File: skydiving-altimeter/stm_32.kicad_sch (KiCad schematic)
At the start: 11 parts, among them J1 Conn_ARM_JTAG_SWD_10, J4 10118193-0001LF, U1 STM32F103C8Tx

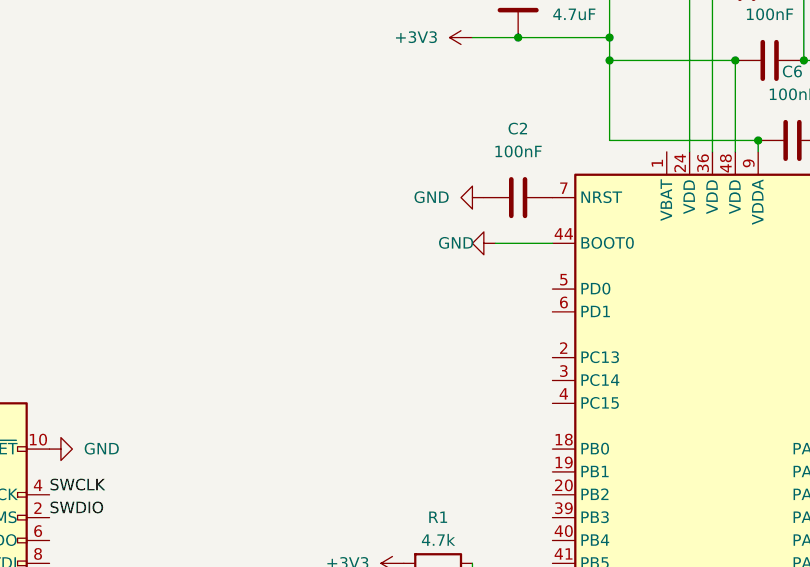
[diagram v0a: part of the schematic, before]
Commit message: Added external resonator to allow usb
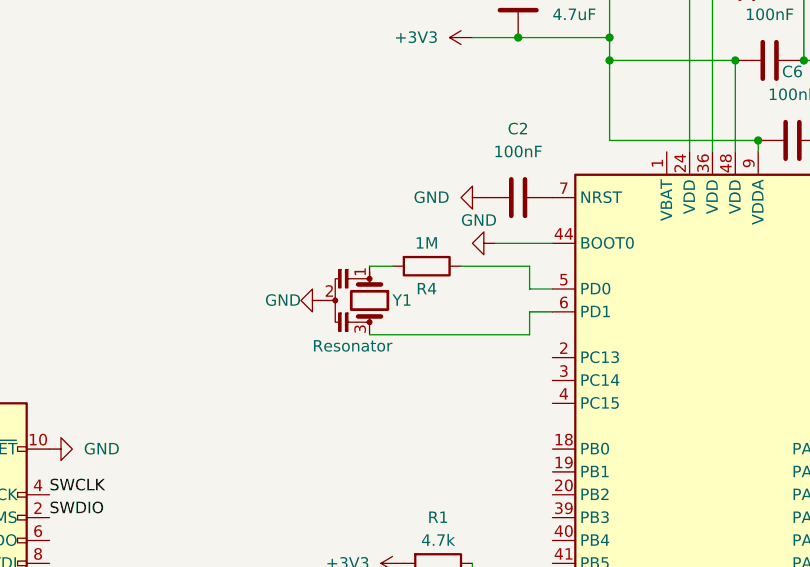
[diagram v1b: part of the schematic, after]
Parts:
- added R4: 1M, Resistor_SMD:R_0805_2012Metric, symbol Device:R
- added Y1: Resonator, JGC42-8828A_CSTNE10M0G550000R0:JGC42-8828A_CSTNE10M0G550000R0, symbol Device:Resonator
- J4: footprint AMPHENOL_10118193-0001LF -> Micro USB Port:AMPHENOL_10118193-0001LF
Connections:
- net GND: now also Y1.2
- net at U1.5 (PD0): now also R4.1
- net at U1.6 (PD1): now also Y1.3
- new net: R4.2, Y1.1
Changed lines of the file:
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@@
   (junction (at 146.05 121.92) (diameter 0) (color 0 0 0 0)
   )
+  (wire (pts (xy 152.4 86.36) (xy 152.4 83.82))
+    (stroke (width 0) (type default))
+  )
   (wire (pts (xy 146.05 121.92) (xy 154.94 121.92))
     (stroke (width 0) (type default))
   )
+  (wire (pts (xy 152.4 88.9) (xy 154.94 88.9))
+    (stroke (width 0) (type default))
+  )
   (wire (pts (xy 161.29 43.18) (xy 170.18 43.18))
     (stroke (width 0) (type default))
@@
     (stroke (width 0) (type default))
   )
+  (wire (pts (xy 134.62 91.44) (xy 152.4 91.44))
+    (stroke (width 0) (type default))
+  )
   (wire (pts (xy 182.88 60.96) (xy 182.88 52.07))
     (stroke (width 0) (type default))
@@
     (stroke (width 0) (type default))
   )
+  (wire (pts (xy 152.4 91.44) (xy 152.4 88.9))
+    (stroke (width 0) (type default))
+  )
   (wire (pts (xy 161.29 52.07) (xy 161.29 58.42))
     (stroke (width 0) (type default))
@@
     (stroke (width 0) (type default))
   )
+  (wire (pts (xy 144.78 83.82) (xy 152.4 83.82))
+    (stroke (width 0) (type default))
+  )
   (wire (pts (xy 146.05 116.84) (xy 146.05 119.38))
     (stroke (width 0) (type default))
   )
+  (wire (pts (xy 134.62 83.82) (xy 137.16 83.82))
+    (stroke (width 0) (type default))
+  )
   (wire (pts (xy 161.29 60.96) (xy 161.29 69.85))
     (stroke (width 0) (type default))
@@
   )
   (wire (pts (xy 161.29 69.85) (xy 177.8 69.85))
+    (stroke (width 0) (type default))
+  )
+  (wire (pts (xy 152.4 86.36) (xy 154.94 86.36))
     (stroke (width 0) (type default))
   )
@@
         (path "/e63e39d7-6ac0-4ffd-8aa3-1841a4541b55/878c02f1-6e0f-4063-b2fd-d88c4b65f3c1"
           (reference "#PWR0103") (unit 1)
+        )
+      )
+    )
+  )
+  (symbol (lib_name "GND_3") (lib_id "power:GND") (at 129.54 87.63 270) (unit 1)
+    (in_bom yes) (on_board yes) (dnp no)
+    (property "Reference" "#PWR011" (at 123.19 87.63 0)
+      (effects (font (size 1.27 1.27)) hide)
+    )
+    (property "Value" "GND" (at 127 87.63 90)
+      (effects (font (size 1.27 1.27)) (justify right))
+    )
+    (property "Footprint" "" (at 129.54 87.63 0)
+      (effects (font (size 1.27 1.27)) hide)
+    )
+    (property "Datasheet" "" (at 129.54 87.63 0)
+      (effects (font (size 1.27 1.27)) hide)
+    )
+    (pin "1")
+    (instances
+      (project "skydiving-altimeter"
+        (path "/e63e39d7-6ac0-4ffd-8aa3-1841a4541b55/878c02f1-6e0f-4063-b2fd-d88c4b65f3c1"
+          (reference "#PWR011") (unit 1)
         )
       )
@@
       (effects (font (size 1.27 1.27)) hide)
     )
-    (property "Value" "GND" (at 142.24 81.28 90)
+    (property "Value" "GND" (at 144.78 78.74 90)
       (effects (font (size 1.27 1.27)) (justify left))
     )
@@
     )
   )
+  (symbol (lib_id "Device:Resonator") (at 134.62 87.63 270) (unit 1)
+    (in_bom yes) (on_board yes) (dnp no)
+    (property "Reference" "Y1" (at 137.16 87.63 90)
+      (effects (font (size 1.27 1.27)) (justify left))
+    )
+    (property "Value" "Resonator" (at 128.27 92.71 90)
+      (effects (font (size 1.27 1.27)) (justify left))
+    )
+    (property "Footprint" "JGC42-8828A_CSTNE10M0G550000R0:JGC42-8828A_CSTNE10M0G550000R0" (at 134.62 86.995 0)
+      (effects (font (size 1.27 1.27)) hide)
+    )
+    (property "Datasheet" "~" (at 134.62 86.995 0)
+      (effects (font (size 1.27 1.27)) hide)
+    )
+    (pin "1")
+    (pin "2")
+    (pin "3")
+    (instances
+      (project "skydiving-altimeter"
+        (path "/e63e39d7-6ac0-4ffd-8aa3-1841a4541b55/878c02f1-6e0f-4063-b2fd-d88c4b65f3c1"
+          (reference "Y1") (unit 1)
+        )
+      )
+    )
+  )
   (symbol (lib_id "power:GND") (at 185.42 69.85 90) (unit 1)
     (in_bom yes) (on_board yes) (dnp no) (fields_autoplaced)
@@
     )
   )
+  (symbol (lib_id "Device:R") (at 140.97 83.82 270) (unit 1)
+    (in_bom yes) (on_board yes) (dnp no)
+    (property "Reference" "R4" (at 140.97 86.36 90)
+      (effects (font (size 1.27 1.27)))
+    )
+    (property "Value" "1M" (at 140.97 81.28 90)
+      (effects (font (size 1.27 1.27)))
+    )
+    (property "Footprint" "Resistor_SMD:R_0805_2012Metric" (at 140.97 82.042 90)
+      (effects (font (size 1.27 1.27)) hide)
+    )
+    (property "Datasheet" "~" (at 140.97 83.82 0)
+      (effects (font (size 1.27 1.27)) hide)
+    )
+    (pin "1")
+    (pin "2")
+    (instances
+      (project "skydiving-altimeter"
+        (path "/e63e39d7-6ac0-4ffd-8aa3-1841a4541b55/878c02f1-6e0f-4063-b2fd-d88c4b65f3c1"
+          (reference "R4") (unit 1)
+        )
+      )
+    )
+  )
   (symbol (lib_id "Device:C") (at 151.13 54.61 0) (unit 1)
     (in_bom yes) (on_board yes) (dnp no) (fields_autoplaced)
@@
       (effects (font (size 1.27 1.27)) (justify left))
     )
-    (property "Footprint" "AMPHENOL_10118193-0001LF" (at 220.98 137.16 0)
+    (property "Footprint" "Micro USB Port:AMPHENOL_10118193-0001LF" (at 220.98 137.16 0)
       (effects (font (size 1.27 1.27)) (justify bottom) hide)
     )

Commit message: Mostly rerouted
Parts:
- removed J4: 10118193-0001LF, Micro USB Port:AMPHENOL_10118193-0001LF, symbol 10118193-0001LF:10118193-0001LF
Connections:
- net M_TX: now reaches U1.30 (PA9)
- net M_RX: now reaches U1.31 (PA10)
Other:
- added sheet USB (usb.kicad_sch)
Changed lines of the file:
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@@
+    (stroke (width 0) (type default))
+  )
+  (wire (pts (xy 248.92 95.25) (xy 252.73 95.25))
     (stroke (width 0) (type default))
   )
@@
     (stroke (width 0) (type default))
   )
+  (wire (pts (xy 248.92 92.71) (xy 252.73 92.71))
+    (stroke (width 0) (type default))
+  )
   (wire (pts (xy 182.88 60.96) (xy 182.88 52.07))
     (stroke (width 0) (type default))
   )
-  (wire (pts (xy 187.96 134.62) (xy 210.82 134.62))
-    (stroke (width 0) (type default))
-  )
   (wire (pts (xy 151.13 58.42) (xy 161.29 58.42))
     (stroke (width 0) (type default))
@@
     (stroke (width 0) (type default))
   )
-  (wire (pts (xy 187.96 132.08) (xy 210.82 132.08))
-    (stroke (width 0) (type default))
-  )
   (wire (pts (xy 152.4 91.44) (xy 152.4 88.9))
     (stroke (width 0) (type default))
@@
     (stroke (width 0) (type default))
   )
+  (wire (pts (xy 190.5 127) (xy 187.96 127))
+    (stroke (width 0) (type default))
+  )
   (wire (pts (xy 161.29 69.85) (xy 177.8 69.85))
     (stroke (width 0) (type default))
@@
   )
   (wire (pts (xy 167.64 147.32) (xy 170.18 147.32))
+    (stroke (width 0) (type default))
+  )
+  (wire (pts (xy 190.5 129.54) (xy 187.96 129.54))
     (stroke (width 0) (type default))
   )
@@
     (effects (font (size 1.27 1.27)) (justify left bottom))
   )
+  (label "M_RX" (at 248.92 95.25 180) (fields_autoplaced)
+    (effects (font (size 1.27 1.27)) (justify right bottom))
+  )
+  (label "M_RX" (at 190.5 129.54 0) (fields_autoplaced)
+    (effects (font (size 1.27 1.27)) (justify left bottom))
+  )
+  (label "M_TX" (at 248.92 92.71 180) (fields_autoplaced)
+    (effects (font (size 1.27 1.27)) (justify right bottom))
+  )
   (label "SWDIO" (at 191.77 137.16 0) (fields_autoplaced)
+    (effects (font (size 1.27 1.27)) (justify left bottom))
+  )
+  (label "M_TX" (at 190.5 127 0) (fields_autoplaced)
     (effects (font (size 1.27 1.27)) (justify left bottom))
   )
@@
     )
   )
-  (symbol (lib_name "GND_1") (lib_id "power:GND") (at 210.82 139.7 270) (unit 1)
-    (in_bom yes) (on_board yes) (dnp no) (fields_autoplaced)
-    (property "Reference" "#PWR09" (at 204.47 139.7 0)
-      (effects (font (size 1.27 1.27)) hide)
-    )
-    (property "Value" "GND" (at 207.01 140.335 90)
-      (effects (font (size 1.27 1.27)) (justify right))
-    )
-    (property "Footprint" "" (at 210.82 139.7 0)
-      (effects (font (size 1.27 1.27)) hide)
-    )
-    (property "Datasheet" "" (at 210.82 139.7 0)
-      (effects (font (size 1.27 1.27)) hide)
-    )
-    (pin "1")
-    (instances
-      (project "skydiving-altimeter"
-        (path "/e63e39d7-6ac0-4ffd-8aa3-1841a4541b55/878c02f1-6e0f-4063-b2fd-d88c4b65f3c1"
-          (reference "#PWR09") (unit 1)
-        )
-      )
-    )
-  )
   (symbol (lib_id "power:+3V3") (at 138.43 116.84 90) (unit 1)
     (in_bom yes) (on_board yes) (dnp no) (fields_autoplaced)
@@
     )
   )
-  (symbol (lib_id "10118193-0001LF:10118193-0001LF") (at 220.98 137.16 0) (unit 1)
-    (in_bom yes) (on_board yes) (dnp no) (fields_autoplaced)
-    (property "Reference" "J4" (at 227.33 136.525 0)
-      (effects (font (size 1.27 1.27)) (justify left))
-    )
-    (property "Value" "10118193-0001LF" (at 227.33 139.065 0)
-      (effects (font (size 1.27 1.27)) (justify left))
-    )
-    (property "Footprint" "Micro USB Port:AMPHENOL_10118193-0001LF" (at 220.98 137.16 0)
-      (effects (font (size 1.27 1.27)) (justify bottom) hide)
-    )
-    (property "Datasheet" "" (at 220.98 137.16 0)
-      (effects (font (size 1.27 1.27)) hide)
-    )
-    (property "PARTREV" "E" (at 220.98 137.16 0)
-      (effects (font (size 1.27 1.27)) (justify bottom) hide)
-    )
-    (property "MANUFACTURER" "Amphenol FCI" (at 220.98 137.16 0)
-      (effects (font (size 1.27 1.27)) (justify bottom) hide)
-    )
-    (property "MAXIMUM_PACKAGE_HEIGHT" "2.55 mm" (at 220.98 137.16 0)
-      (effects (font (size 1.27 1.27)) (justify bottom) hide)
-    )
-    (property "STANDARD" "Manufacturer Recommendations" (at 220.98 137.16 0)
-      (effects (font (size 1.27 1.27)) (justify bottom) hide)
-    )
-    (pin "1")
-    (pin "2")
-    (pin "3")
-    (pin "4")
-    (pin "5")
-    (pin "S1")
-    (pin "S2")
-    (pin "S3")
-    (pin "S4")
-    (pin "S5")
-    (pin "S6")
-    (instances
-      (project "skydiving-altimeter"
-        (path "/e63e39d7-6ac0-4ffd-8aa3-1841a4541b55/878c02f1-6e0f-4063-b2fd-d88c4b65f3c1"
-          (reference "J4") (unit 1)
-        )
-      )
-    )
-  )
-  (symbol (lib_id "power:+5V") (at 210.82 129.54 90) (unit 1)
-    (in_bom yes) (on_board yes) (dnp no) (fields_autoplaced)
-    (property "Reference" "#PWR08" (at 214.63 129.54 0)
-      (effects (font (size 1.27 1.27)) hide)
-    )
-    (property "Value" "+5V" (at 207.01 130.175 90)
-      (effects (font (size 1.27 1.27)) (justify left))
-    )
-    (property "Footprint" "" (at 210.82 129.54 0)
-      (effects (font (size 1.27 1.27)) hide)
-    )
-    (property "Datasheet" "" (at 210.82 129.54 0)
-      (effects (font (size 1.27 1.27)) hide)
-    )
-    (pin "1")
-    (instances
-      (project "skydiving-altimeter"
-        (path "/e63e39d7-6ac0-4ffd-8aa3-1841a4541b55/878c02f1-6e0f-4063-b2fd-d88c4b65f3c1"
-          (reference "#PWR08") (unit 1)
-        )
-      )
-    )
-  )
   (symbol (lib_id "power:+3V3") (at 146.05 58.42 90) (unit 1)
     (in_bom yes) (on_board yes) (dnp no) (fields_autoplaced)
@@
         (path "/e63e39d7-6ac0-4ffd-8aa3-1841a4541b55/878c02f1-6e0f-4063-b2fd-d88c4b65f3c1"
           (reference "#PWR0108") (unit 1)
-        )
-      )
-    )
-  )
-  (symbol (lib_name "GND_2") (lib_id "power:GND") (at 210.82 144.78 270) (unit 1)
-    (in_bom yes) (on_board yes) (dnp no) (fields_autoplaced)
-    (property "Reference" "#PWR010" (at 204.47 144.78 0)
-      (effects (font (size 1.27 1.27)) hide)
-    )
-    (property "Value" "GND" (at 207.01 145.415 90)
-      (effects (font (size 1.27 1.27)) (justify right))
-    )
-    (property "Footprint" "" (at 210.82 144.78 0)
-      (effects (font (size 1.27 1.27)) hide)
-    )
-    (property "Datasheet" "" (at 210.82 144.78 0)
-      (effects (font (size 1.27 1.27)) hide)
-    )
-    (pin "1")
-    (instances
-      (project "skydiving-altimeter"
-        (path "/e63e39d7-6ac0-4ffd-8aa3-1841a4541b55/878c02f1-6e0f-4063-b2fd-d88c4b65f3c1"
-          (reference "#PWR010") (unit 1)
         )
       )
@@
       )
     )
+  )
+  (sheet (at 252.73 90.17) (size 12.7 7.62) (fields_autoplaced)
+    (stroke (width 0.1524) (type solid))
+    (fill (color 0 0 0 0.0000))
+    (property "Sheetname" "USB" (at 252.73 89.4584 0)
+      (effects (font (size 1.27 1.27)) (justify left bottom))
+    )
+    (property "Sheetfile" "usb.kicad_sch" (at 252.73 98.3746 0)
+      (effects (font (size 1.27 1.27)) (justify left top))
+    )
+    (pin "RX" input (at 252.73 92.71 180)
+      (effects (font (size 1.27 1.27)) (justify left))
+    )
+    (pin "TX" input (at 252.73 95.25 180)
+      (effects (font (size 1.27 1.27)) (justify left))
+    )
+    (instances
+      (project "skydiving-altimeter"
+        (path "/e63e39d7-6ac0-4ffd-8aa3-1841a4541b55/878c02f1-6e0f-4063-b2fd-d88c4b65f3c1" (page "5"))
+      )
+    )
